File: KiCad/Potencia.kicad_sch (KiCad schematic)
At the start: 64 parts, among them J1 Conn_01x02, J11 Conn_01x02, J12 Conn_01x02, J3-4 Conn_01x02, J5 Conn_01x02, J7-8 Conn_01x02, J9 Conn_01x02, K1 G6E, K10 G6E, K2 G6E, K3 G6E, K4 G6E, K5 G6E, K6 G6E, K7 G6E, K8 G6E, K9 G6E, Q1 NMOS, Q10 NMOS, Q11 IRLZ44N, Q12 IRLZ44N, Q2 NMOS, Q3 NMOS, Q4 NMOS, Q5 NMOS, Q6 NMOS, Q7 NMOS, Q8 NMOS, Q9 NMOS, U4 ${SIM.PARAMS}, U5 ${SIM.PARAMS}

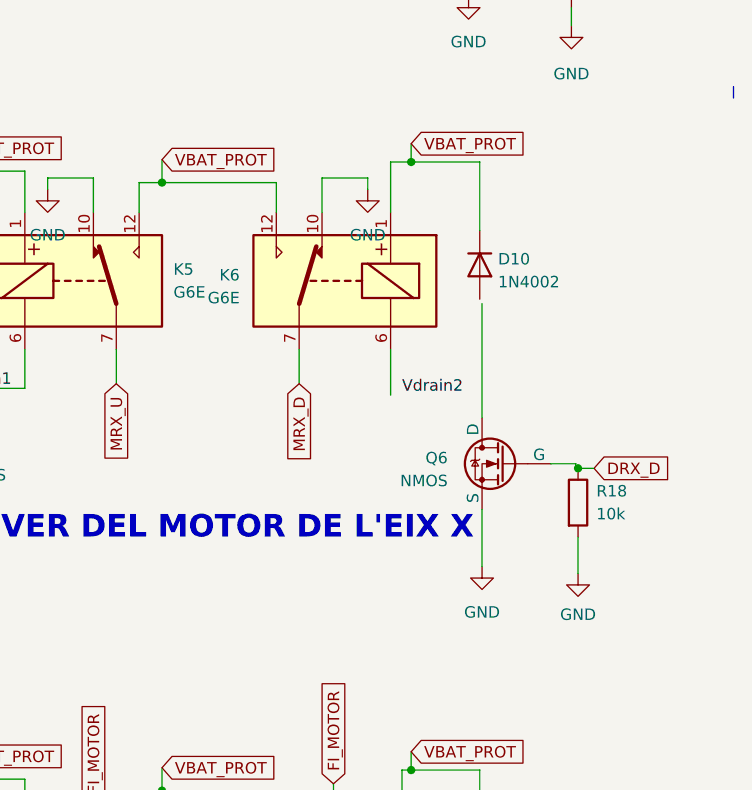
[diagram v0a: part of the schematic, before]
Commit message: afegit esquematic (testpoints + extensor de pines) falta acabar placement
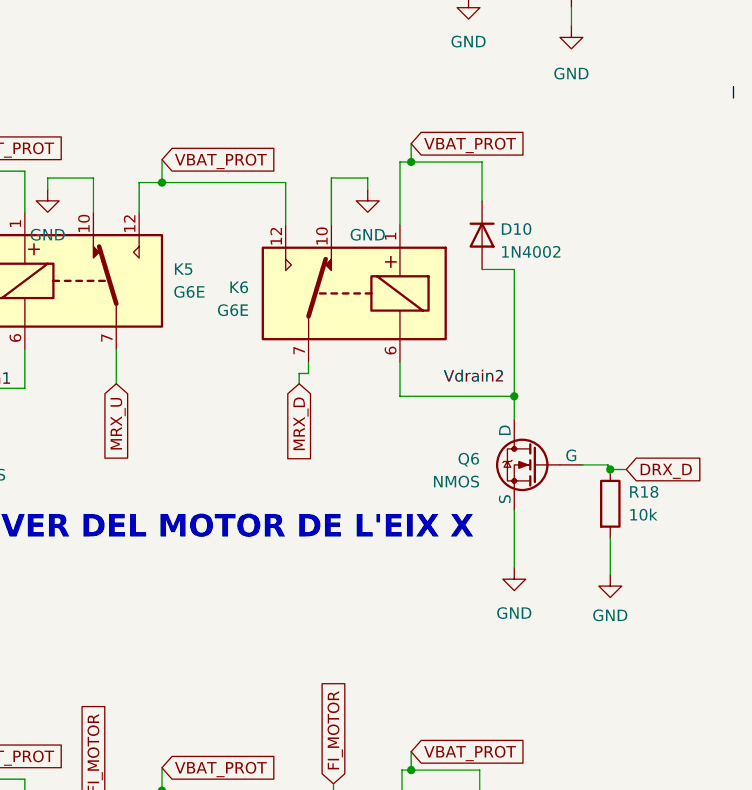
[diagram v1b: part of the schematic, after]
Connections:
- net at D10.2 (A): now also K6.6, Q6.1 (D)
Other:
- moved on the sheet: D10, K6, Q6, R18

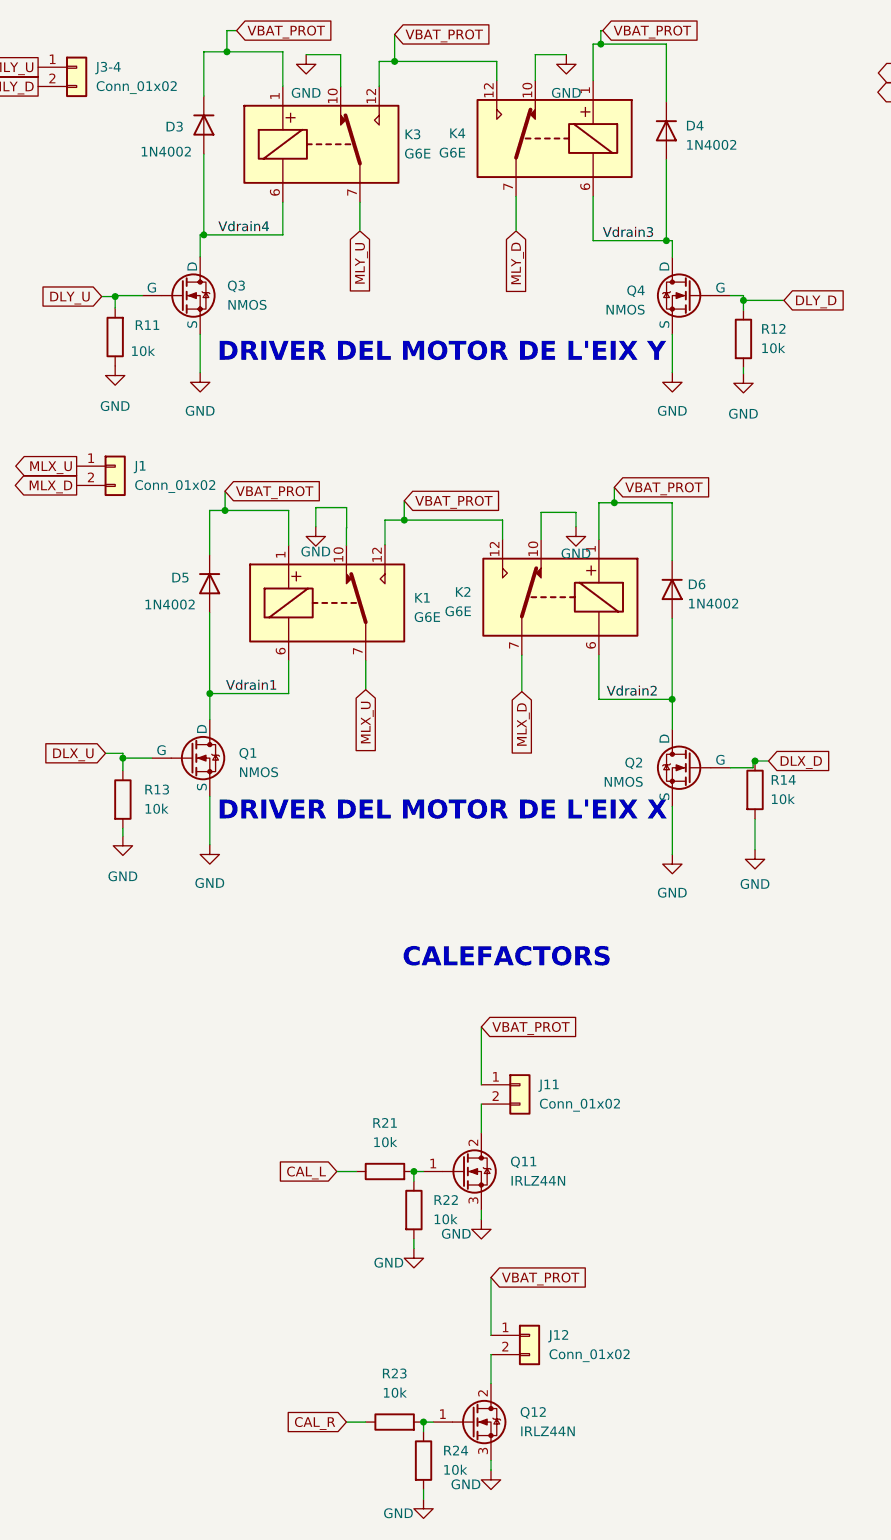
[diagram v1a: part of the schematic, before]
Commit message: final de pcb, falta els test points
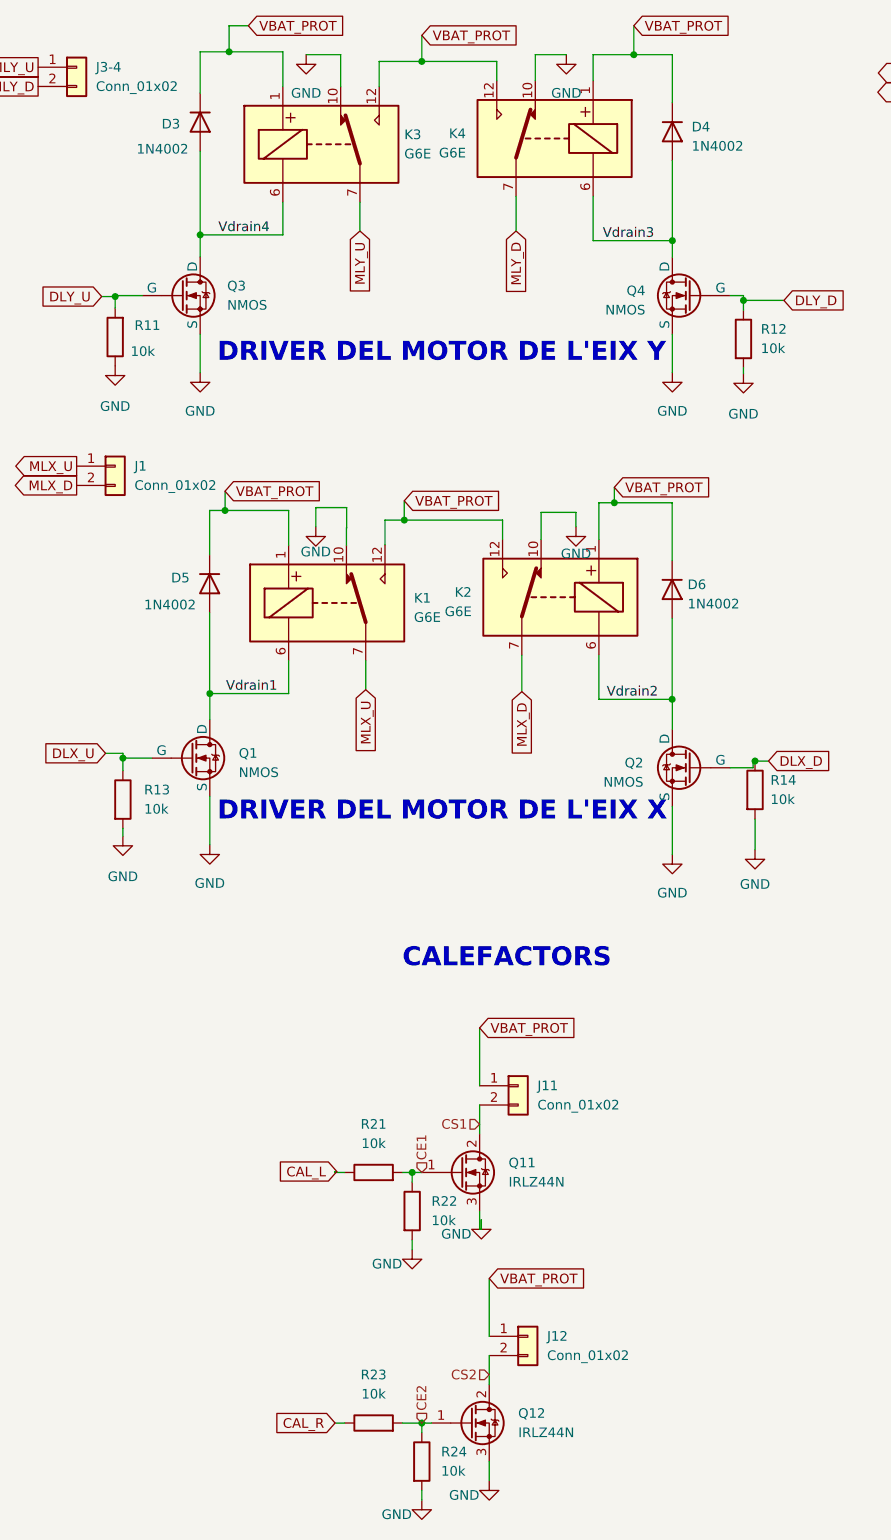
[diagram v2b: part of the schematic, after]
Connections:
- net CE2: now reaches Q12.1 (G), R23.2, R24.1
- net CE1: now reaches Q11.1 (G), R21.2, R22.1
- net CS1: now reaches J11.2 (Pin_2), Q11.2 (D)
- net CS2: now reaches J12.2 (Pin_2), Q12.2 (D)
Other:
- moved on the sheet: D3, D4, R21, R23

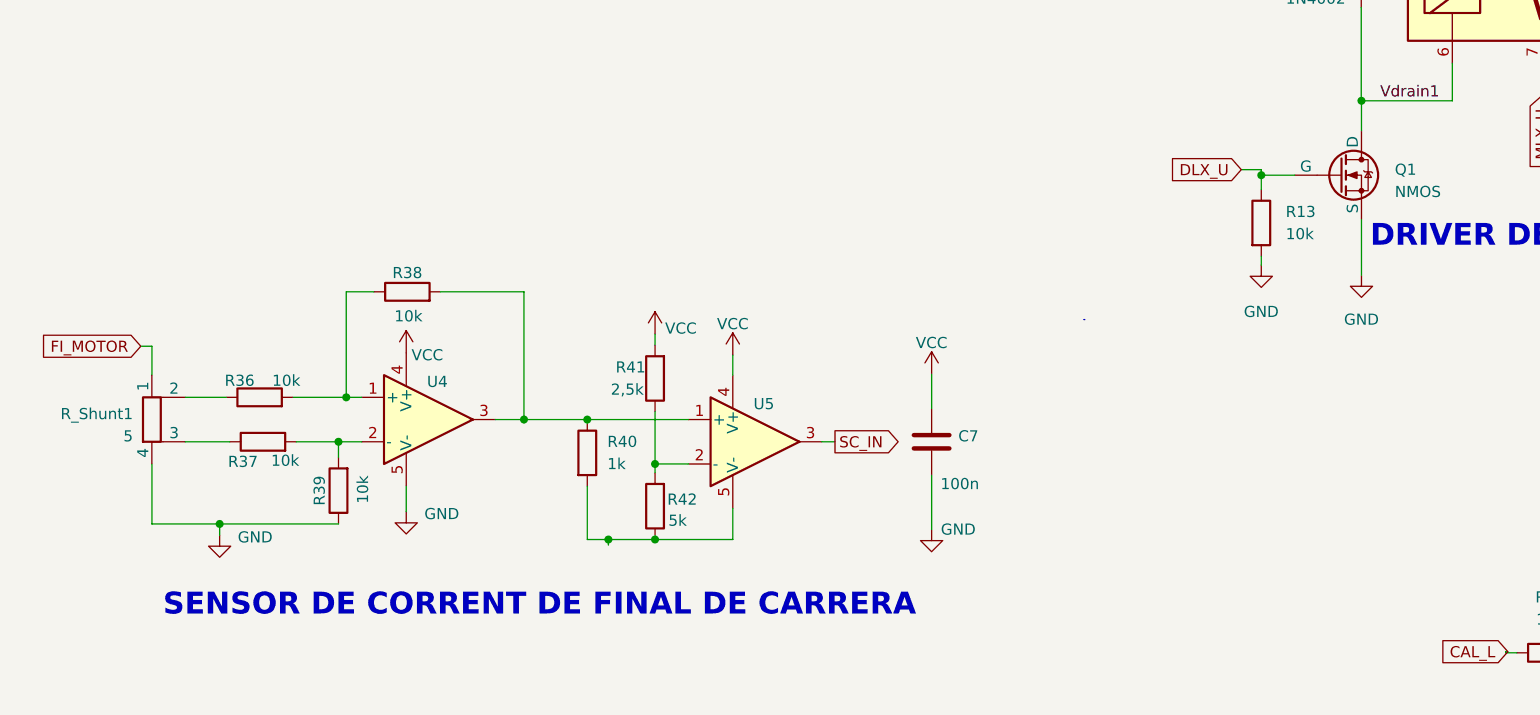
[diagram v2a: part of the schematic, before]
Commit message: petites modificacions resistencies part digital + resolucio errors pcb
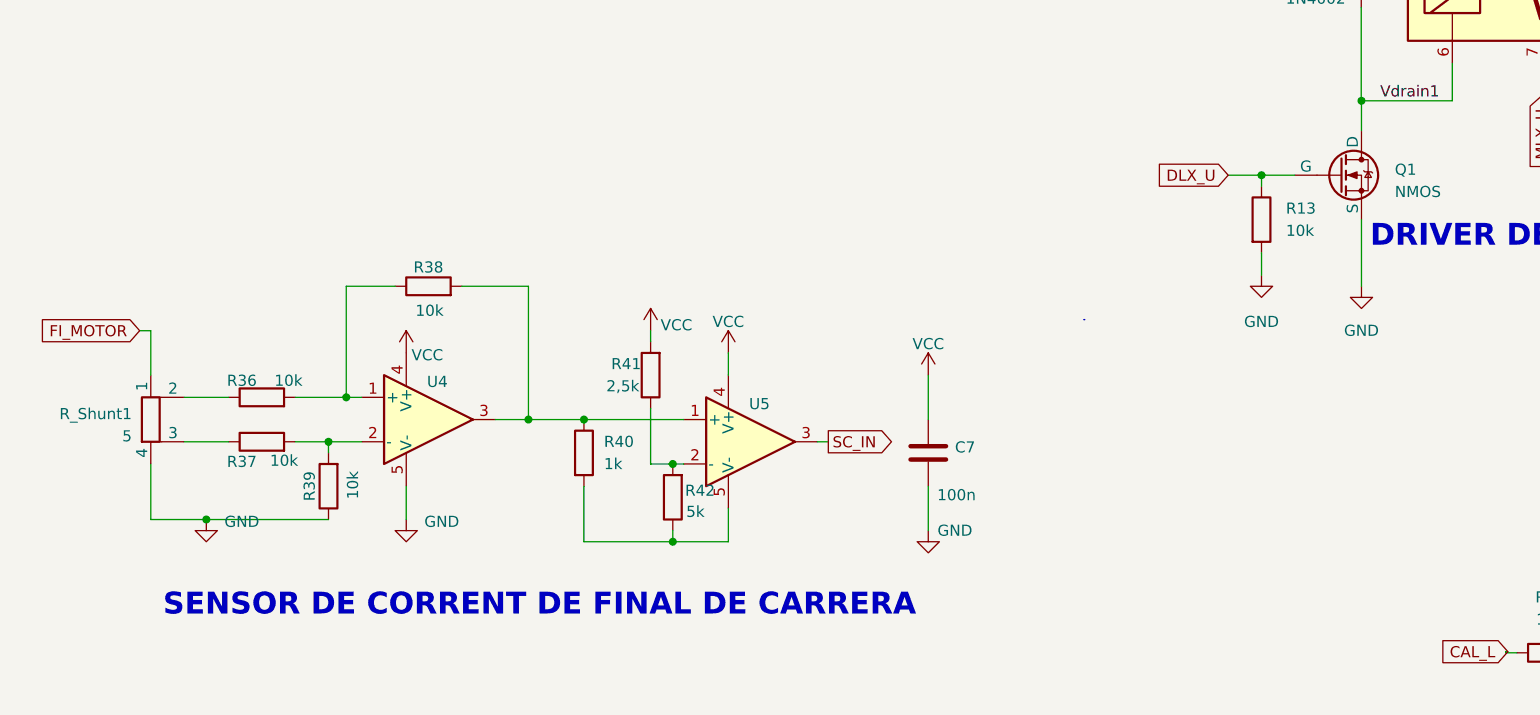
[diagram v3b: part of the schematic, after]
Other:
- moved on the sheet: C7, R38, R39, R41, R42, U5

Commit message: canvis pcb finals
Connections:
- net GND: now also R40.2, R42.1, U5.5 (V-)
- net Vdrain1: no longer D12.2 (A), D8.2 (A), K5.6, K9.6, Q5.1 (D), Q9.1 (D)
- net Vdrain2: no longer D13.2 (A), K10.6, Q10.1 (D)
- net Vdrain3: now also D3.2 (A), K3.6, Q3.1 (D); no longer D11.2 (A), D4.2 (A), K4.6, K8.6, Q4.1 (D), Q8.1 (D)
- net Vdrain4: now also D4.2 (A), K4.6, Q4.1 (D); no longer D3.2 (A), D9.2 (A), K3.6, K7.6, Q3.1 (D), Q7.1 (D)
- new net Vdrain10: D13.2 (A), K10.6, Q10.1 (D)
- new net Vdrain5: D8.2 (A), K5.6, Q5.1 (D)
- new net Vdrain7: D9.2 (A), K7.6, Q7.1 (D)
- new net Vdrain8: D11.2 (A), K8.6, Q8.1 (D)
- new net Vdrain9: D12.2 (A), K9.6, Q9.1 (D)
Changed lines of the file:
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@@
 	)
 	(junction
+		(at 90.17 167.64)
+		(diameter 0)
+		(color 0 0 0 0)
+	)
+	(junction
 		(at 285.7246 193.04)
 		(diameter 0)
@@
 	(wire
 		(pts
+			(xy 90.17 167.64) (xy 99.06 167.64)
+		)
+		(stroke
+			(width 0)
+			(type default)
+		)
+	)
+	(wire
+		(pts
 			(xy 105.41 167.64) (xy 105.41 163.83)
 		)
@@
 	(wire
 		(pts
-			(xy 88.9 167.64) (xy 99.06 167.64)
+			(xy 88.9 167.64) (xy 90.17 167.64)
 		)
 		(stroke
@@
 		)
 	)
-	(label "Vdrain2"
+	(label "Vdrain10"
 		(at 349.4786 185.547 0)
 		(effects
@@
 		)
 	)
-	(label "Vdrain4"
+	(label "Vdrain3"
 		(at 178.9176 56.769 0)
 		(effects
@@
 		)
 	)
-	(label "Vdrain1"
+	(label "Vdrain9"
 		(at 299.3136 184.785 0)
 		(effects
@@
 		)
 	)
-	(label "Vdrain1"
+	(label "Vdrain5"
 		(at 299.3136 117.221 0)
 		(effects
@@
 		)
 	)
-	(label "Vdrain3"
+	(label "Vdrain8"
 		(at 348.4626 58.293 0)
 		(effects
@@
 		)
 	)
-	(label "Vdrain4"
+	(label "Vdrain7"
 		(at 297.7896 57.531 0)
 		(effects
@@
 		)
 	)
-	(label "Vdrain3"
+	(label "Vdrain4"
 		(at 229.5906 57.531 0)
 		(effects
@@
 		)
 	)
-	(label "Vdrain2"
+	(label "Vdrain6"
 		(at 354.1014 116.967 0)
 		(effects
@@
 					(unit 1)
 				)
+			)
+		)
+	)
+	(symbol
+		(lib_id "power:GND")
+		(at 90.17 167.64 0)
+		(unit 1)
+		(exclude_from_sim no)
+		(in_bom yes)
+		(on_board yes)
+		(dnp no)
+		(property "Reference" "#PWR030"
+			(at 90.17 173.99 0)
+			(effects
+				(font
+					(size 1.27 1.27)
+				)
+				(hide yes)
+			)
+		)
+		(property "Value" "GND"
+			(at 94.234 167.894 0)
+			(effects
+				(font
+					(size 1.27 1.27)
+				)
+			)
+		)
+		(property "Footprint" ""
+			(at 90.17 167.64 0)
+			(effects
+				(font
+					(size 1.27 1.27)
+				)
+				(hide yes)
+			)
+		)
+		(property "Datasheet" ""
+			(at 90.17 167.64 0)
+			(effects
+				(font
+					(size 1.27 1.27)
+				)
+				(hide yes)
+			)
+		)
+		(property "Description" ""
+			(at 90.17 167.64 0)
+			(effects
+				(font
+					(size 1.27 1.27)
+				)
+			)
+		)
+		(pin "1"
+		)
+		(instances
+			(project "Retrovisors_Carlos_Soler_Ingrid_Lopez"
+				(path "/a9cf8edd-cd44-4958-b775-951afc8c27af/bcd2f2ee-8367-4dc4-b798-6c0c11179178"
+					(reference "#PWR030")
+					(unit 1)
+				)

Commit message: pcb definitiva
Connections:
- net Vdrain6: now also D10.2 (A), K6.6, Q6.1 (D)
- net RSH2: now reaches R36.1, R_Shunt1.2
- net RSH3: now reaches R37.1, R_Shunt1.3
- net O2V-: now reaches R41.1, R42.2, U5.2 (-)
- net O2V+: now reaches R38.2, R40.1, U4.3, U5.1 (+)
- net O1V+: now reaches R36.2, R38.1, U4.1 (+)
- net O1V-: now reaches R37.2, R39.2, U4.2 (-)
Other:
- note added: "25/05/2026"
- note added: "Aqui podem veure el microcontrolador y les seves conexions, tambe esta la botonera per tal de poder moure els retrovisors."
- note added: "Etapa Digital"
- moved on the sheet: R39
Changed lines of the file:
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@@
 	(generator_version "9.0")
 	(paper "A3")
+	(text "25/05/2026\n"
+		(exclude_from_sim no)
+		(at 336.55 280.416 0)
+		(effects
+			(font
+				(size 1.27 1.27)
+			)
+		)
+	)
+	(text "Aqui podem veure el microcontrolador y les seves conexions,\ntambe esta la botonera per tal de poder moure els retrovisors."
+		(exclude_from_sim no)
+		(at 301.498 256.032 0)
+		(effects
+			(font
+				(size 1.27 1.27)
+			)
+			(justify left)
+		)
+	)
 	(text "DRIVER DEL MOTOR DE OBRIR I TENCAR\n\n"
 		(exclude_from_sim no)
@@
 		)
 	)
+	(text "Etapa Digital\n\n"
+		(exclude_from_sim no)
+		(at 315.214 277.876 0)
+		(effects
+			(font
+				(size 1.27 1.27)
+			)
+		)
+	)
 	(text "DRIVER DEL MOTOR DE L'EIX Y\n"
 		(exclude_from_sim no)
@@
 	)
 	(junction
-		(at 61.722 151.13)
+		(at 88.9 153.67)
 		(diameter 0)
 		(color 0 0 0 0)
 	)
 	(junction
-		(at 59.69 156.21)
-		(diameter 0)
-		(color 0 0 0 0)
-	)
-	(junction
-		(at 88.9 153.67)
+		(at 59.69 151.13)
 		(diameter 0)
 		(color 0 0 0 0)
@@
 	)
 	(junction
+		(at 57.15 156.21)
+		(diameter 0)
+		(color 0 0 0 0)
+	)
+	(junction
 		(at 372.618 126.238)
 		(diameter 0)
@@
 	(wire
 		(pts
-			(xy 61.722 138.43) (xy 61.722 151.13)
+			(xy 59.69 138.43) (xy 59.69 151.13)
 		)
 		(stroke
@@
 	(wire
 		(pts
-			(xy 45.72 165.1) (xy 59.69 165.1)
+			(xy 45.72 165.1) (xy 57.15 165.1)
 		)
 		(stroke
@@
 	(wire
 		(pts
-			(xy 55.88 151.13) (xy 61.722 151.13)
+			(xy 55.88 151.13) (xy 59.69 151.13)
 		)
 		(stroke
@@
 	(wire
 		(pts
+			(xy 59.69 151.13) (xy 63.5 151.13)
+		)
+		(stroke
+			(width 0)
+			(type default)
+		)
+	)
+	(wire
+		(pts
 			(xy 238.76 69.85) (xy 238.76 74.93)
 		)
@@
 	(wire
 		(pts
-			(xy 59.69 156.21) (xy 63.5 156.21)
-		)
-		(stroke
-			(width 0)
-			(type default)
-		)
-	)
-	(wire
-		(pts
 			(xy 372.364 126.238) (xy 372.364 125.73)
 		)
@@
 	(wire
 		(pts
-			(xy 67.31 138.43) (xy 61.722 138.43)
+			(xy 67.31 138.43) (xy 59.69 138.43)
 		)
 		(stroke
@@
 	(wire
 		(pts
-			(xy 59.69 157.48) (xy 59.69 156.21)
+			(xy 57.15 157.48) (xy 57.15 156.21)
 		)
 		(stroke
@@
 	(wire
 		(pts
-			(xy 61.722 151.13) (xy 63.5 151.13)
-		)
-		(stroke
-			(width 0)
-			(type default)
-		)
-	)
-	(wire
-		(pts
 			(xy 180.34 29.21) (xy 180.34 32.639)
 		)
@@
 	(wire
 		(pts
+			(xy 57.15 156.21) (xy 63.5 156.21)
+		)
+		(stroke
+			(width 0)
+			(type default)
+		)
+	)
+	(wire
+		(pts
 			(xy 176.53 59.69) (xy 176.53 56.769)
 		)
@@
 	(wire
 		(pts
-			(xy 55.88 156.21) (xy 59.69 156.21)
+			(xy 55.88 156.21) (xy 57.15 156.21)
 		)
 		(stroke
@@
 		)
 	)
+	(label "RSH3"
+		(at 45.72 156.21 270)
+		(effects
+			(font
+				(size 1.27 1.27)
+			)
+			(justify right bottom)
+		)
+	)
 	(label "Vdrain10"
 		(at 349.4786 185.547 0)
@@
 		)
 	)
+	(label "RSH2"
+		(at 46.99 151.13 90)
+		(effects
+			(font
+				(size 1.27 1.27)
+			)
+			(justify left bottom)
+		)
+	)
+	(label "CE2"
+		(at 205.74 213.36 90)
+		(effects
+			(font
+				(size 1.27 1.27)
+			)
+			(justify left bottom)
+		)
+	)
 	(label "Vdrain3"
 		(at 178.9176 56.769 0)
@@
 		)
 	)
+	(label "O1V+"
+		(at 63.5 151.13 90)
+		(effects
+			(font
+				(size 1.27 1.27)
+			)
+			(justify left bottom)
+		)
+	)
 	(label "Vdrain9"
 		(at 299.3136 184.785 0)
@@
 		)
 	)
+	(label "CS1"
+		(at 213.36 173.99 180)
+		(effects
+			(font
+				(size 1.27 1.27)
+			)
+			(justify right bottom)
+		)
+	)
 	(label "Vdrain8"
 		(at 348.4626 58.293 0)
@@
 		)
 	)
+	(label "O2V-"
+		(at 96.52 158.75 270)
+		(effects
+			(font
+				(size 1.27 1.27)
+			)
+			(justify right bottom)
+		)
+	)
 	(label "Vdrain7"
 		(at 297.7896 57.531 0)
@@
 		)
 	)
+	(label "O1V-"
+		(at 62.23 156.21 270)
+		(effects
+			(font
+				(size 1.27 1.27)
+			)
+			(justify right bottom)
+		)
+	)
+	(label "CS2"
+		(at 214.63 207.01 180)
+		(effects
+			(font
+				(size 1.27 1.27)
+			)
+			(justify right bottom)
+		)
+	)
 	(label "Vdrain4"
 		(at 229.5906 57.531 0)
@@
 		)
 	)
+	(label "CE1"
+		(at 204.47 180.34 90)
+		(effects
+			(font
+				(size 1.27 1.27)
+			)
+			(justify left bottom)
+		)
+	)
 	(label "Vdrain1"
 		(at 179.9336 117.221 0)
@@
 		)
 	)
+	(label "O2V+"
+		(at 100.33 153.67 90)
+		(effects
+			(font
+				(size 1.27 1.27)
+			)
+			(justify left bottom)
+		)
+	)
 	(label "Vdrain6"
-		(at 354.1014 116.967 0)
+		(at 354.33 118.11 0)
 		(effects
 			(font
@@
 		)
 	)
-	(hierarchical_label "CS2"
-		(shape input)
-		(at 214.63 207.01 180)
-		(effects
-			(font
-				(size 1.27 1.27)
-			)
-			(justify right)
-		)
-	)
-	(hierarchical_label "CS1"
-		(shape input)
-		(at 213.36 173.99 180)
-		(effects
-			(font
-				(size 1.27 1.27)
-			)
-			(justify right)
-		)
-	)
-	(hierarchical_label "CE1"
-		(shape input)
-		(at 205.74 180.34 90)
-		(effects
-			(font
-				(size 1.27 1.27)
-			)
-			(justify left)
-		)
-	)
-	(hierarchical_label "CE2"
-		(shape input)
-		(at 205.74 213.36 90)
-		(effects
-			(font
-				(size 1.27 1.27)
-			)
-			(justify left)
-		)
-	)
 	(symbol
 		(lib_id "Device:R_Shunt")
@@
 	(symbol
 		(lib_id "Device:R")
-		(at 59.69 161.29 180)
+		(at 57.15 161.29 180)
 		(unit 1)
 		(exclude_from_sim no)
@@
 		(dnp no)
 		(property "Reference" "R39"
-			(at 57.531 161.29 90)
+			(at 54.991 161.29 90)
 			(effects
 				(font
@@
 		)
 		(property "Value" "10k"
-			(at 62.484 161.163 90)
+			(at 59.182 161.544 90)
 			(effects
 				(font
@@
 		)
 		(property "Footprint" "Resistor_SMD:R_1206_3216Metric_Pad1.30x1.75mm_HandSolder"
-			(at 61.468 161.29 90)
+			(at 58.928 161.29 90)
 			(effects
 				(font
@@
 		)
 		(property "Datasheet" "~"
-			(at 59.69 161.29 0)
+			(at 57.15 161.29 0)
 			(effects
 				(font
@@
 		)
 		(property "Description" ""
-			(at 59.69 161.29 0)
+			(at 57.15 161.29 0)
 			(effects
 				(font

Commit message: diseny final final
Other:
- moved on the sheet: D12, D13, D6, J9, K10, K2, K9, Q10, Q9, R19, R20

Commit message: afegit tot final
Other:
- note added: "Etapa de potència"
- note removed: "Aqui podem veure el microcontrolador y les seves conexions, tambe esta la botonera per tal de poder moure els retrovisors."
- note removed: "Etapa Digital"
- moved on the sheet: C7, J11, J12, Q11, Q12, R21, R22, R23, R24, R36, R37, R38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
